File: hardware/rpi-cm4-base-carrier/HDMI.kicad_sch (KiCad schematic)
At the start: 4 parts, among them J7 690-019-298-412, U7 RT9742SNGV

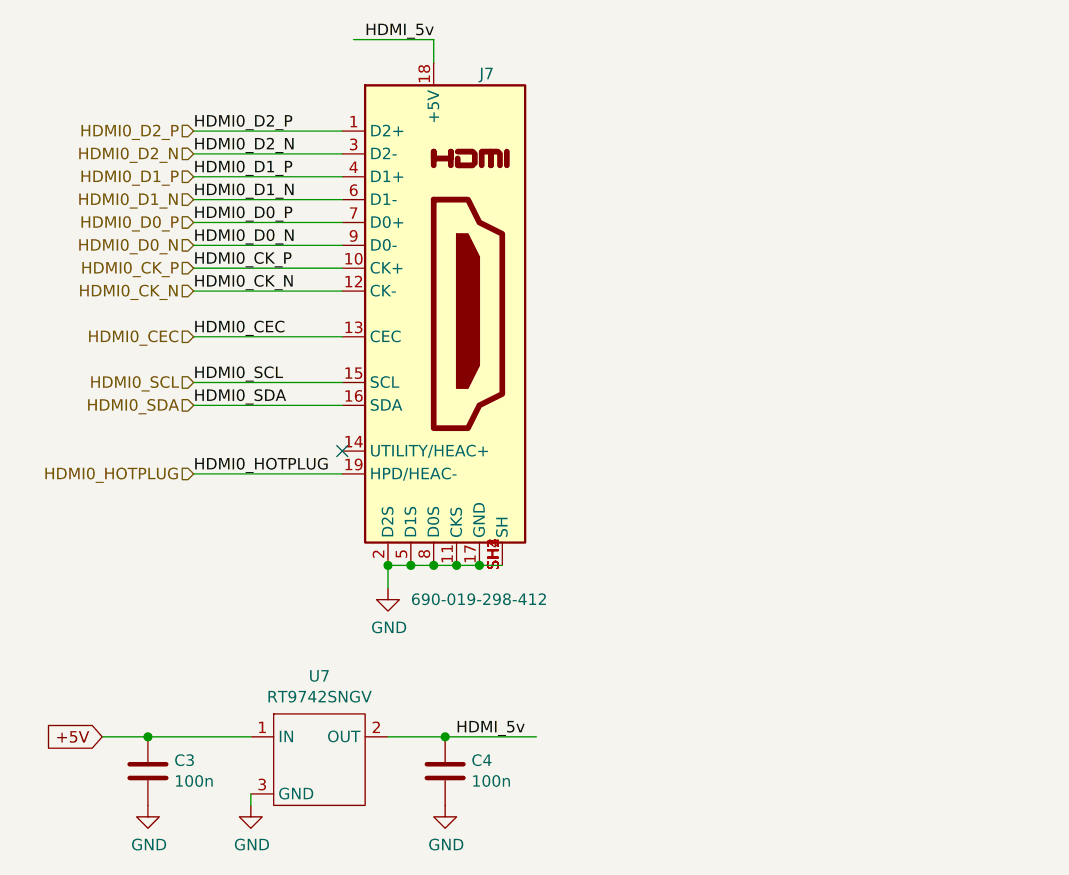
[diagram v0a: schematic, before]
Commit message: routing for some modules progressing quickly, USBHUB mostly complete, thought needed regarding which connectors should be exposed post assembly and which should be for internal use only. LED identifiers and buttons still missing
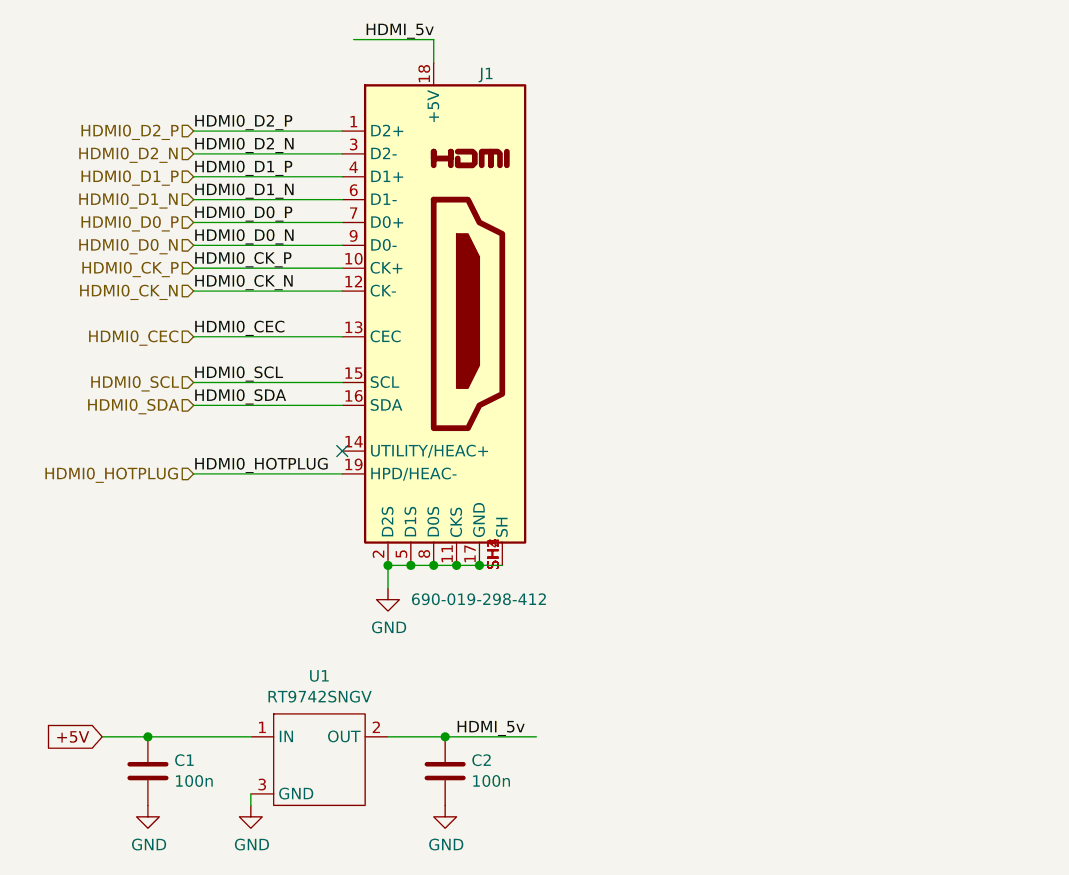
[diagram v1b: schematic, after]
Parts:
- renumbered C3 to C1, C4 to C2, J7 to J1, U7 to U1
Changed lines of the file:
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@@
   (symbol (lib_id "power:GND") (at 68.58 82.55 0) (unit 1)
     (in_bom yes) (on_board yes) (dnp no)
-    (property "Reference" "#PWR08" (at 68.58 88.9 0)
+    (property "Reference" "#PWR03" (at 68.58 88.9 0)
       (effects (font (size 1.27 1.27)) hide)
     )
@@
       (project "rpi-cm4-base-carrier"
         (path "/92c58705-ecb0-498b-b561-44a3f0daad57/caa71f4c-454d-4ac9-b287-456eafb34991/e4c63a9a-1194-4ada-8eb9-090df9cdb15a"
-          (reference "#PWR010") (unit 1)
+          (reference "#PWR03") (unit 1)
         )
       )
@@
   (symbol (lib_id "Device:C") (at 74.93 102.87 0) (unit 1)
     (in_bom yes) (on_board yes) (dnp no)
-    (property "Reference" "C4" (at 77.851 101.7016 0)
+    (property "Reference" "C2" (at 77.851 101.7016 0)
       (effects (font (size 1.27 1.27)) (justify left))
     )
@@
       (project "rpi-cm4-base-carrier"
         (path "/92c58705-ecb0-498b-b561-44a3f0daad57/caa71f4c-454d-4ac9-b287-456eafb34991/e4c63a9a-1194-4ada-8eb9-090df9cdb15a"
-          (reference "C4") (unit 1)
+          (reference "C2") (unit 1)
         )
       )
@@
   (symbol (lib_id "power:GND") (at 53.34 106.68 0) (unit 1)
     (in_bom yes) (on_board yes) (dnp no)
-    (property "Reference" "#PWR010" (at 53.34 113.03 0)
+    (property "Reference" "#PWR02" (at 53.34 113.03 0)
       (effects (font (size 1.27 1.27)) hide)
     )
@@
       (project "rpi-cm4-base-carrier"
         (path "/92c58705-ecb0-498b-b561-44a3f0daad57/caa71f4c-454d-4ac9-b287-456eafb34991/e4c63a9a-1194-4ada-8eb9-090df9cdb15a"
-          (reference "#PWR09") (unit 1)
+          (reference "#PWR02") (unit 1)
         )
       )
@@
   (symbol (lib_id "CM4IO:RT9742SNGV") (at 58.42 102.87 0) (unit 1)
     (in_bom yes) (on_board yes) (dnp no)
-    (property "Reference" "U7" (at 60.96 92.329 0)
+    (property "Reference" "U1" (at 60.96 92.329 0)
       (effects (font (size 1.27 1.27)))
     )
@@
       (project "rpi-cm4-base-carrier"
         (path "/92c58705-ecb0-498b-b561-44a3f0daad57/caa71f4c-454d-4ac9-b287-456eafb34991/e4c63a9a-1194-4ada-8eb9-090df9cdb15a"
-          (reference "U7") (unit 1)
+          (reference "U1") (unit 1)
         )
       )
@@
   (symbol (lib_id "Device:C") (at 41.91 102.87 0) (unit 1)
     (in_bom yes) (on_board yes) (dnp no)
-    (property "Reference" "C3" (at 44.831 101.7016 0)
+    (property "Reference" "C1" (at 44.831 101.7016 0)
       (effects (font (size 1.27 1.27)) (justify left))
     )
@@
       (project "rpi-cm4-base-carrier"
         (path "/92c58705-ecb0-498b-b561-44a3f0daad57/caa71f4c-454d-4ac9-b287-456eafb34991/e4c63a9a-1194-4ada-8eb9-090df9cdb15a"
-          (reference "C3") (unit 1)
+          (reference "C1") (unit 1)
         )
       )
@@
   (symbol (lib_id "power:GND") (at 74.93 106.68 0) (unit 1)
     (in_bom yes) (on_board yes) (dnp no)
-    (property "Reference" "#PWR011" (at 74.93 113.03 0)
+    (property "Reference" "#PWR04" (at 74.93 113.03 0)
       (effects (font (size 1.27 1.27)) hide)
     )
@@
       (project "rpi-cm4-base-carrier"
         (path "/92c58705-ecb0-498b-b561-44a3f0daad57/caa71f4c-454d-4ac9-b287-456eafb34991/e4c63a9a-1194-4ada-8eb9-090df9cdb15a"
-          (reference "#PWR011") (unit 1)
+          (reference "#PWR04") (unit 1)
         )
       )
@@
   (symbol (lib_id "CM4IO:HDMI_A_1.4") (at 73.66 52.07 0) (unit 1)
     (in_bom yes) (on_board yes) (dnp no)
-    (property "Reference" "J7" (at 78.74 25.4 0)
+    (property "Reference" "J1" (at 78.74 25.4 0)
       (effects (font (size 1.27 1.27)) (justify left))
     )
@@
       (project "rpi-cm4-base-carrier"
         (path "/92c58705-ecb0-498b-b561-44a3f0daad57/caa71f4c-454d-4ac9-b287-456eafb34991/e4c63a9a-1194-4ada-8eb9-090df9cdb15a"
-          (reference "J7") (unit 1)
+          (reference "J1") (unit 1)
         )
       )
@@
   (symbol (lib_id "power:GND") (at 41.91 106.68 0) (unit 1)
     (in_bom yes) (on_board yes) (dnp no)
-    (property "Reference" "#PWR09" (at 41.91 113.03 0)
+    (property "Reference" "#PWR01" (at 41.91 113.03 0)
       (effects (font (size 1.27 1.27)) hide)
     )
@@
       (project "rpi-cm4-base-carrier"
         (path "/92c58705-ecb0-498b-b561-44a3f0daad57/caa71f4c-454d-4ac9-b287-456eafb34991/e4c63a9a-1194-4ada-8eb9-090df9cdb15a"
-          (reference "#PWR08") (unit 1)
-        )
-      )
+          (reference "#PWR01") (unit 1)
+        )
+      )

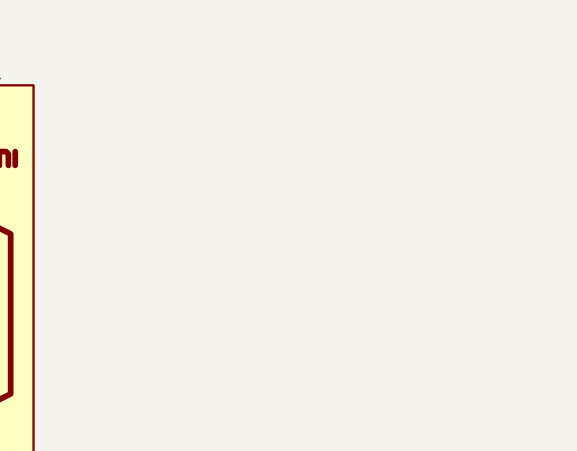
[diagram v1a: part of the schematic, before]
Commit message: most diff pairs routed, forgot about intra-pair spacing
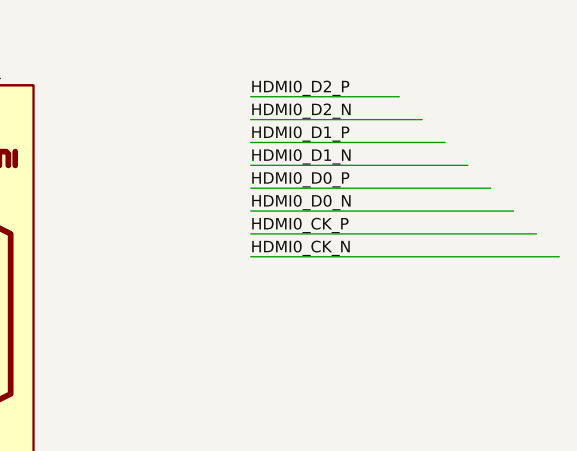
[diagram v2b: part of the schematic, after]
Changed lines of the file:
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@@
+    (stroke (width 0) (type solid))
+  )
+  (wire (pts (xy 107.95 40.64) (xy 137.16 40.64))
     (stroke (width 0) (type solid))
   )
@@
     (stroke (width 0) (type solid))
   )
+  (wire (pts (xy 107.95 43.18) (xy 139.7 43.18))
+    (stroke (width 0) (type solid))
+  )
+  (wire (pts (xy 107.95 45.72) (xy 142.24 45.72))
+    (stroke (width 0) (type solid))
+  )
   (wire (pts (xy 73.66 21.59) (xy 73.66 24.13))
     (stroke (width 0) (type solid))
@@
     (stroke (width 0) (type solid))
   )
+  (wire (pts (xy 107.95 33.02) (xy 129.54 33.02))
+    (stroke (width 0) (type solid))
+  )
   (wire (pts (xy 46.99 46.99) (xy 63.5 46.99))
     (stroke (width 0) (type solid))
@@
     (stroke (width 0) (type solid))
   )
+  (wire (pts (xy 107.95 27.94) (xy 124.46 27.94))
+    (stroke (width 0) (type solid))
+  )
   (wire (pts (xy 46.99 62.23) (xy 63.5 62.23))
     (stroke (width 0) (type solid))
   )
+  (wire (pts (xy 107.95 35.56) (xy 132.08 35.56))
+    (stroke (width 0) (type solid))
+  )
   (wire (pts (xy 46.99 31.75) (xy 63.5 31.75))
     (stroke (width 0) (type solid))
@@
     (stroke (width 0) (type solid))
   )
+  (wire (pts (xy 107.95 30.48) (xy 127 30.48))
+    (stroke (width 0) (type solid))
+  )
   (wire (pts (xy 46.99 59.69) (xy 63.5 59.69))
     (stroke (width 0) (type solid))
@@
     (stroke (width 0) (type solid))
   )
+  (wire (pts (xy 107.95 38.1) (xy 134.62 38.1))
+    (stroke (width 0) (type solid))
+  )
   (wire (pts (xy 46.99 39.37) (xy 63.5 39.37))
     (stroke (width 0) (type solid))
@@
     (effects (font (size 1.27 1.27)) (justify left bottom))
   )
+  (label "HDMI0_D0_N" (at 107.95 40.64 0) (fields_autoplaced)
+    (effects (font (size 1.27 1.27)) (justify left bottom))
+  )
   (label "HDMI0_CEC" (at 46.99 54.61 0) (fields_autoplaced)
     (effects (font (size 1.27 1.27)) (justify left bottom))
   )
+  (label "HDMI0_CK_P" (at 107.95 43.18 0) (fields_autoplaced)
+    (effects (font (size 1.27 1.27)) (justify left bottom))
+  )
+  (label "HDMI0_D2_P" (at 107.95 27.94 0) (fields_autoplaced)
+    (effects (font (size 1.27 1.27)) (justify left bottom))
+  )
+  (label "HDMI0_D2_N" (at 107.95 30.48 0) (fields_autoplaced)
+    (effects (font (size 1.27 1.27)) (justify left bottom))
+  )
   (label "HDMI0_SDA" (at 46.99 62.23 0) (fields_autoplaced)
+    (effects (font (size 1.27 1.27)) (justify left bottom))
+  )
+  (label "HDMI0_D1_N" (at 107.95 35.56 0) (fields_autoplaced)
+    (effects (font (size 1.27 1.27)) (justify left bottom))
+  )
+  (label "HDMI0_D1_P" (at 107.95 33.02 0) (fields_autoplaced)
+    (effects (font (size 1.27 1.27)) (justify left bottom))
+  )
+  (label "HDMI0_D0_P" (at 107.95 38.1 0) (fields_autoplaced)
     (effects (font (size 1.27 1.27)) (justify left bottom))
   )
@@
     (effects (font (size 1.27 1.27)) (justify left bottom))
   )
+  (label "HDMI0_CK_N" (at 107.95 45.72 0) (fields_autoplaced)
+    (effects (font (size 1.27 1.27)) (justify left bottom))
+  )
   (global_label "+5V" (shape input) (at 36.83 99.06 180) (fields_autoplaced)
     (effects (font (size 1.27 1.27)) (justify right))
@@
     (effects (font (size 1.27 1.27)) (justify right))
   )
+  (netclass_flag "" (length 2.54) (shape round) (at 137.16 40.64 0) (fields_autoplaced)
+    (effects (font (size 1.27 1.27)) (justify left bottom))
+    (property "Netclass" "HDMI 100R Diff" (at 138.049 38.1 0)
+      (effects (font (size 1.27 1.27) italic) (justify left))
+    )
+  )
+  (netclass_flag "" (length 2.54) (shape round) (at 139.7 43.18 0) (fields_autoplaced)
+    (effects (font (size 1.27 1.27)) (justify left bottom))
+    (property "Netclass" "HDMI 100R Diff" (at 140.589 40.64 0)
+      (effects (font (size 1.27 1.27) italic) (justify left))
+    )
+  )
+  (netclass_flag "" (length 2.54) (shape round) (at 127 30.48 0) (fields_autoplaced)
+    (effects (font (size 1.27 1.27)) (justify left bottom))
+    (property "Netclass" "HDMI 100R Diff" (at 127.889 27.94 0)
+      (effects (font (size 1.27 1.27) italic) (justify left))
+    )
+  )
+  (netclass_flag "" (length 2.54) (shape round) (at 134.62 38.1 0) (fields_autoplaced)
+    (effects (font (size 1.27 1.27)) (justify left bottom))
+    (property "Netclass" "HDMI 100R Diff" (at 135.509 35.56 0)
+      (effects (font (size 1.27 1.27) italic) (justify left))
+    )
+  )
+  (netclass_flag "" (length 2.54) (shape round) (at 129.54 33.02 0) (fields_autoplaced)
+    (effects (font (size 1.27 1.27)) (justify left bottom))
+    (property "Netclass" "HDMI 100R Diff" (at 130.429 30.48 0)
+      (effects (font (size 1.27 1.27) italic) (justify left))
+    )
+  )
+  (netclass_flag "" (length 2.54) (shape round) (at 124.46 27.94 0) (fields_autoplaced)
+    (effects (font (size 1.27 1.27)) (justify left bottom))
+    (property "Netclass" "HDMI 100R Diff" (at 125.349 25.4 0)
+      (effects (font (size 1.27 1.27) italic) (justify left))
+    )
+  )
+  (netclass_flag "" (length 2.54) (shape round) (at 142.24 45.72 0) (fields_autoplaced)
+    (effects (font (size 1.27 1.27)) (justify left bottom))
+    (property "Netclass" "HDMI 100R Diff" (at 143.129 43.18 0)
+      (effects (font (size 1.27 1.27) italic) (justify left))
+    )
+  )
+  (netclass_flag "" (length 2.54) (shape round) (at 132.08 35.56 0) (fields_autoplaced)
+    (effects (font (size 1.27 1.27)) (justify left bottom))
+    (property "Netclass" "HDMI 100R Diff" (at 132.969 33.02 0)
+      (effects (font (size 1.27 1.27) italic) (justify left))
+    )
+  )
   (symbol (lib_id "power:GND") (at 68.58 82.55 0) (unit 1)

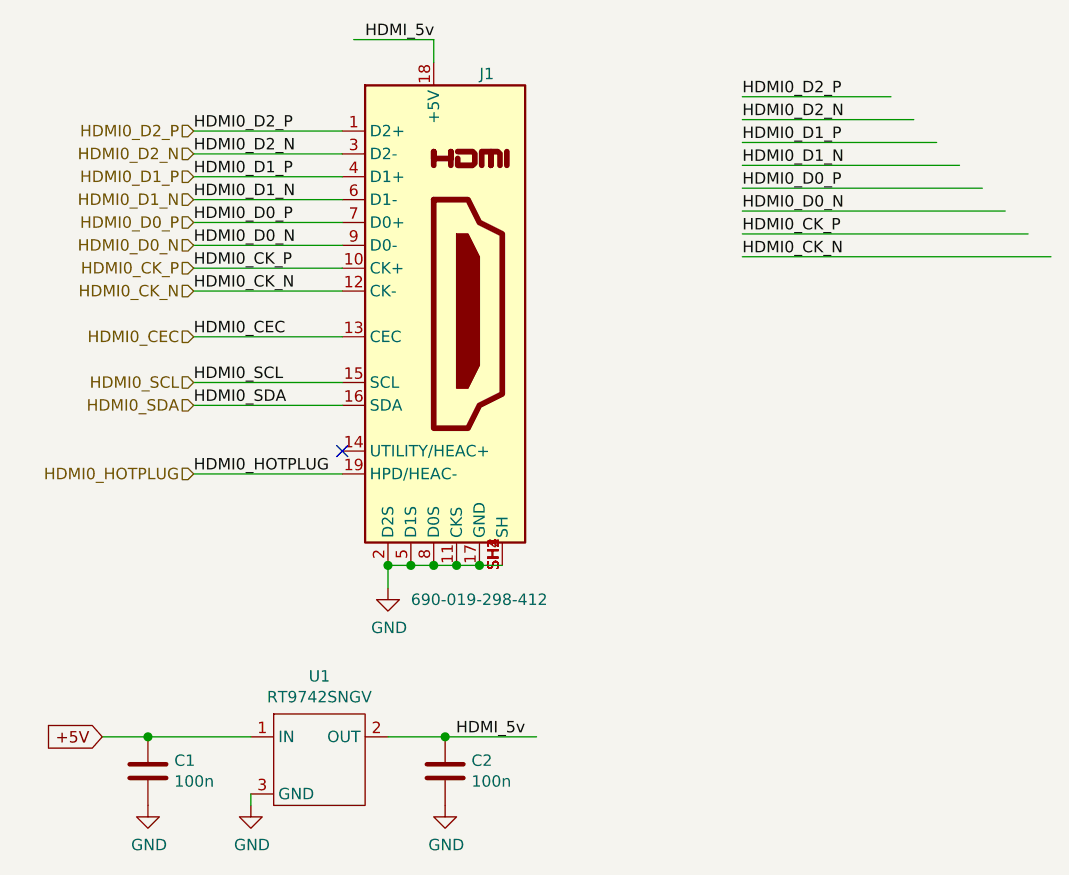
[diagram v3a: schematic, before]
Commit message: design files exported ready for manufacture, LCSC part numbers added throughout the library
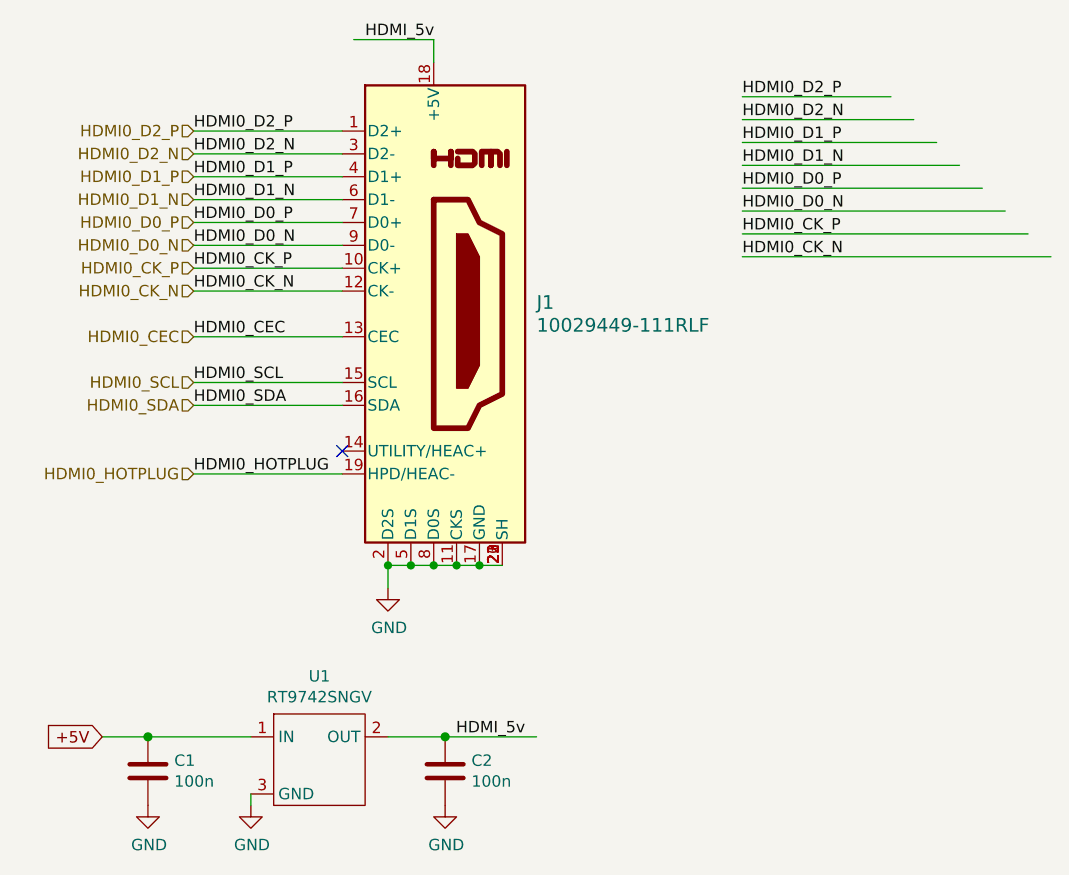
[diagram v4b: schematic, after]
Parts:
- removed J1: 690-019-298-412, CM4IO:EDAC 690-019-298-412, symbol CM4IO:HDMI_A_1.4
- added J1: 10029449-111RLF, CONN_10029449111_AMP, symbol 10029449_111RLF:10029449-111RLF
- C1, C2: LCSC Part # (none) -> C152724; LCSC Part Number (none) -> C152724
- U1: LCSC Part # (none) -> C3235509; LCSC Part Number (none) -> C3235509
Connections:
- net GND: now also J1.11 (CKS), J1.17 (GND), J1.2 (D2S), J1.20 (SH), J1.21 (SH), J1.22 (SH), J1.23 (SH), J1.5 (D1S), J1.8 (D0S)
- net HDMI0_CEC: now also J1.13 (CEC)
- net HDMI0_CK_N: now also J1.12 (CK-)
- net HDMI0_CK_P: now also J1.10 (CK+)
- net HDMI0_D0_N: now also J1.9 (D0-)
- net HDMI0_D0_P: now also J1.7 (D0+)
- net HDMI0_D1_N: now also J1.6 (D1-)
- net HDMI0_D1_P: now also J1.4 (D1+)
- net HDMI0_D2_N: now also J1.3 (D2-)
- net HDMI0_D2_P: now also J1.1 (D2+)
- net HDMI0_HOTPLUG: now also J1.19 (HPD/HEAC-)
- net HDMI0_SCL: now also J1.15 (SCL)
- net HDMI0_SDA: now also J1.16 (SDA)
- net HDMI_5v: now also J1.18 (+5V)
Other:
- title: (none) -> Raspberry Pi Compute Module 4 Control Node
